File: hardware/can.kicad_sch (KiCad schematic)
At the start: 7 parts, among them U2 MCP2542FDxMF

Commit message: values-correction
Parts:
- C7, C8: value 100nF -> 100n
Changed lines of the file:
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@@
 			)
 		)
-		(property "Value" "100nF"
+		(property "Value" "100n"
 			(at 100.33 84.4613 0)
 			(effects
@@
 			)
 		)
-		(property "Value" "100nF"
+		(property "Value" "100n"
 			(at 133.35 83.8262 0)
 			(effects

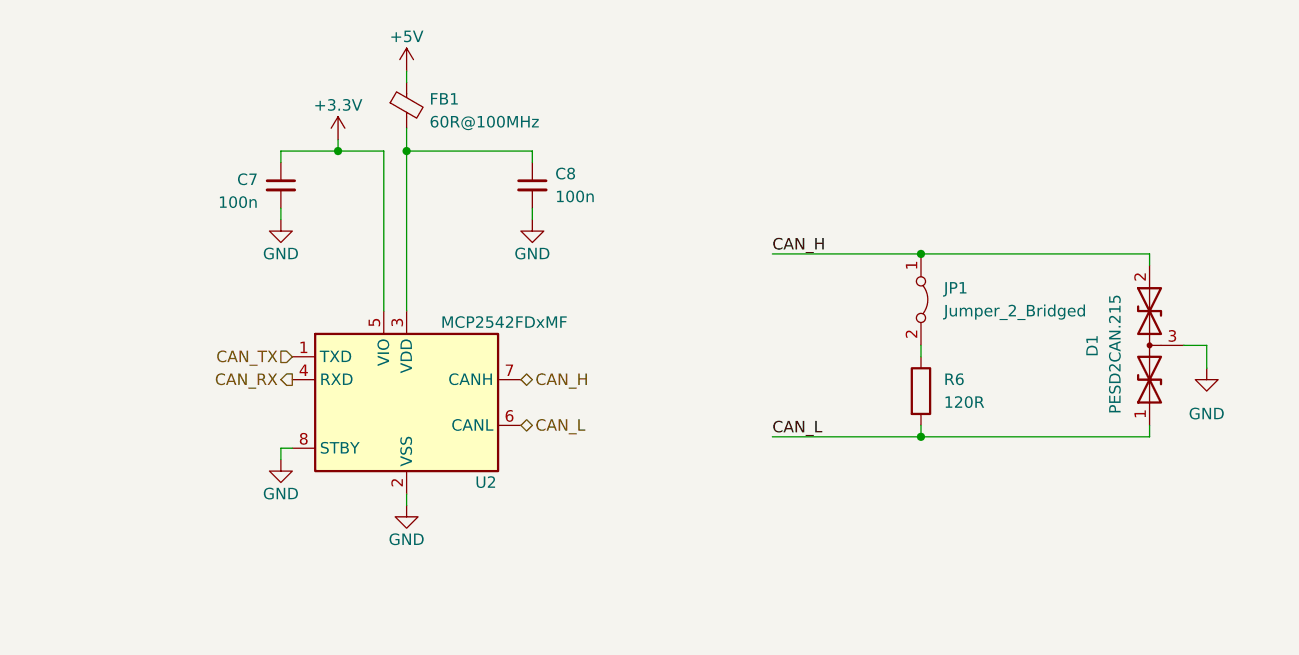
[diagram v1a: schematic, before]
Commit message: added sheet pins
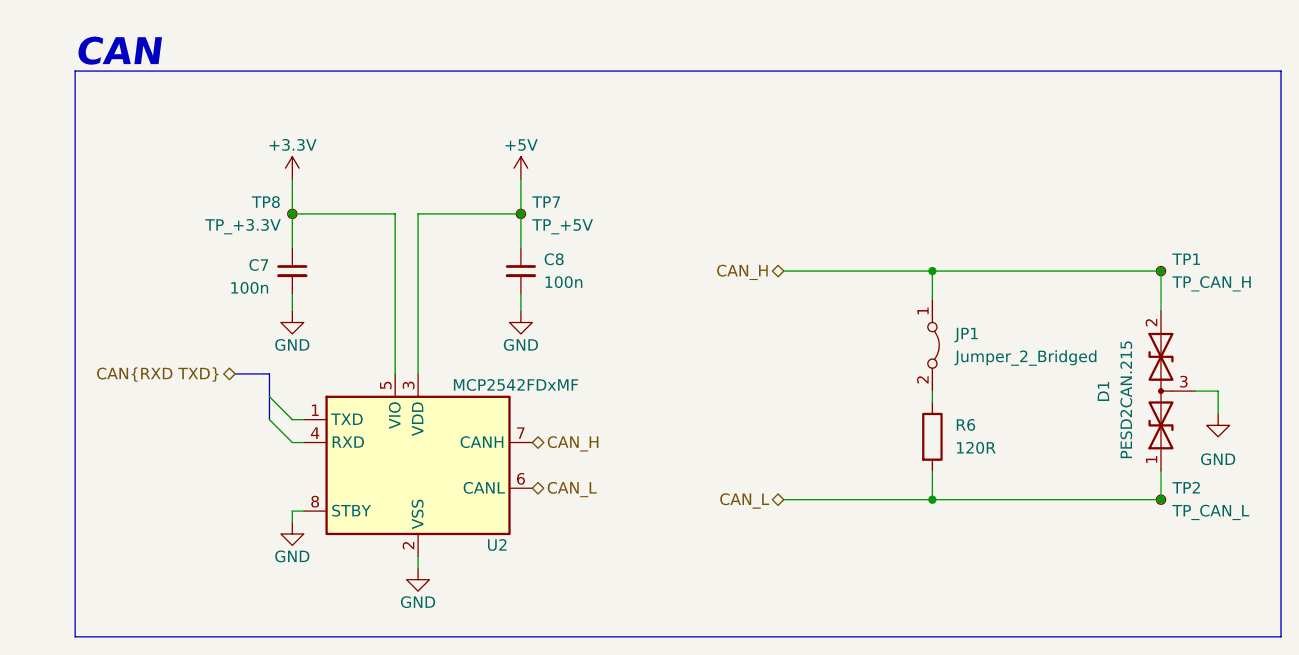
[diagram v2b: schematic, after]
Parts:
- removed FB1: 60R@100MHz, Inductor_SMD:L_0603_1608Metric, symbol Device:FerriteBead_Small
- added TP1: TP_CAN_H, symbol Connector:TestPoint_Small
- added TP2: TP_CAN_L, symbol Connector:TestPoint_Small
- added TP7: TP_+5V, symbol Connector:TestPoint_Small
- added TP8: TP_+3.3V, symbol Connector:TestPoint_Small
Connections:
- net +3.3V: now also TP8.1
- net +5V: now also C8.1, U2.3 (VDD), TP7.1
- net CAN_H: now also TP1.1
- net CAN_L: now also TP2.1
- net CAN_RX: no longer names the net of U2.4 (RXD)
- net CAN_TX: no longer names the net of U2.1 (TXD)
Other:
- note added: "CAN"
- moved on the sheet: C7, C8, D1, JP1, R6, U2

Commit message: added 6V6 for servo
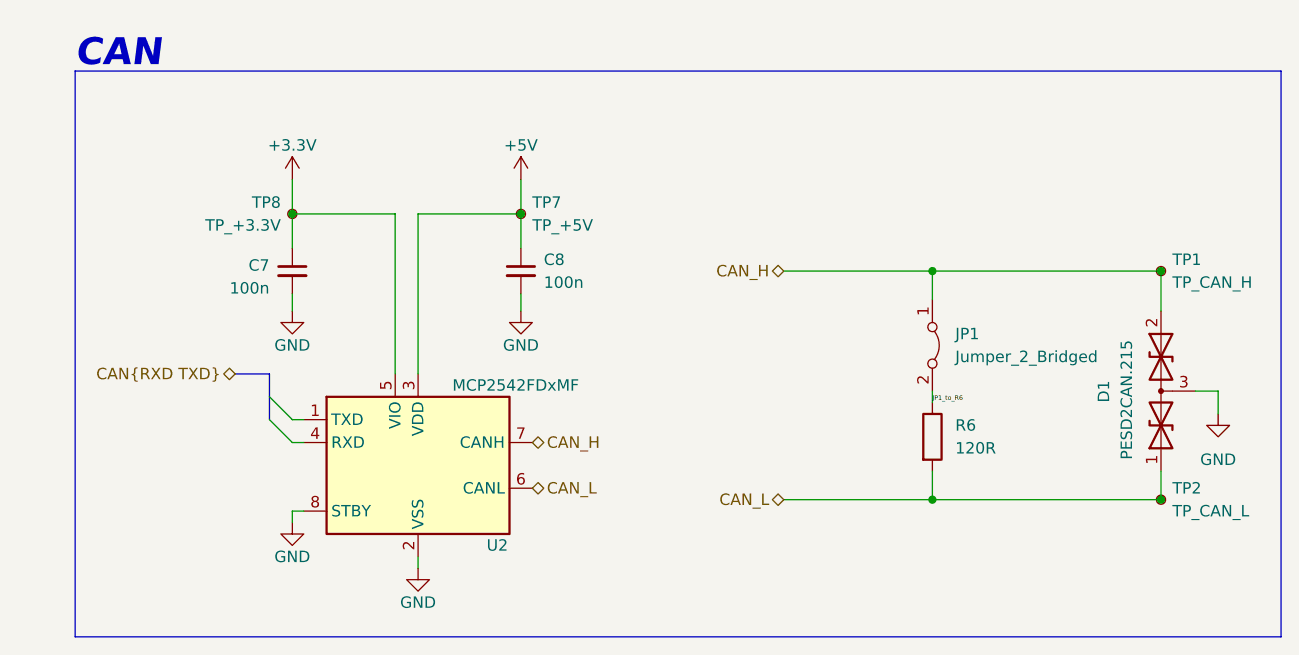
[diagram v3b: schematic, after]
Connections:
- net JP1_to_R6: now reaches JP1.2 (B), R6.1
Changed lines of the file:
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@@
+		)
+	)
+	(label "JP1_to_R6"
+		(at 175.26 106.68 0)
+		(fields_autoplaced yes)
+		(effects
+			(font
+				(size 0.508 0.508)
+			)
+			(justify left bottom)
 		)
 	)

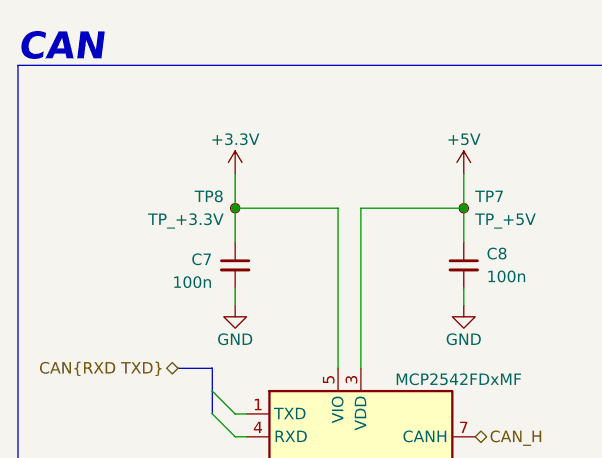
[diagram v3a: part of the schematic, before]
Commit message: connectors - added, buses - todo
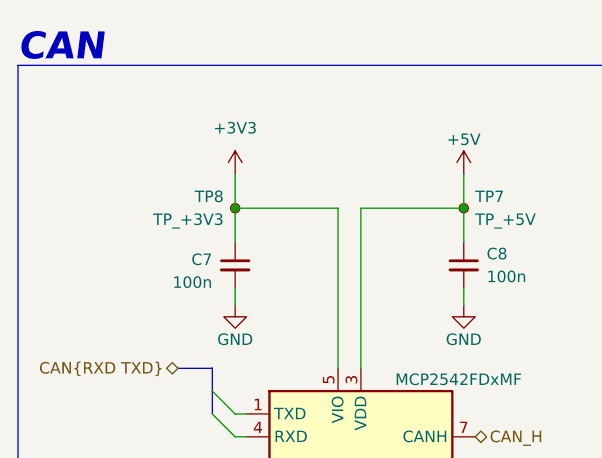
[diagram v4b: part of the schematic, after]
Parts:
- TP8: value TP_+3.3V -> TP_+3V3
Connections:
- net +3.3V renamed +3V3
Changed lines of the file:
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@@
+	)
+	(symbol
+		(lib_id "power:+3V3")
+		(at 104.14 81.915 0)
+		(unit 1)
+		(exclude_from_sim no)
+		(in_bom yes)
+		(on_board yes)
+		(dnp no)
+		(fields_autoplaced yes)
+		(property "Reference" "#PWR014"
+			(at 104.14 85.725 0)
+			(effects
+				(font
+					(size 1.27 1.27)
+				)
+				(hide yes)
+			)
+		)
+		(property "Value" "+3V3"
+			(at 104.14 76.835 0)
+			(effects
+				(font
+					(size 1.27 1.27)
+				)
+			)
+		)
+		(property "Footprint" ""
+			(at 104.14 81.915 0)
+			(effects
+				(font
+					(size 1.27 1.27)
+				)
+				(hide yes)
+			)
+		)
+		(property "Datasheet" ""
+			(at 104.14 81.915 0)
+			(effects
+				(font
+					(size 1.27 1.27)
+				)
+				(hide yes)
+			)
+		)
+		(property "Description" "Power symbol creates a global label with name \"+3V3\""
+			(at 104.14 81.915 0)
+			(effects
+				(font
+					(size 1.27 1.27)
+				)
+				(hide yes)
+			)
+		)
+		(pin "1"
+		)
+		(instances
+			(project "drs"
+				(path "/b652b05a-4e3d-4ad1-b032-18886abe7d45/b1fd2a01-bf35-4031-ba71-28db4e5321a0"
+					(reference "#PWR014")
+					(unit 1)
+				)
+			)
+		)
 	)
 	(symbol
@@
 			)
 		)
-		(property "Value" "TP_+3.3V"
+		(property "Value" "TP_+3V3"
 			(at 102.87 86.9949 0)
 			(effects
@@
 					(unit 1)
 				)
-			)
-		)
-	)
-	(symbol
-		(lib_id "power:+3.3V")
-		(at 104.14 81.915 0)
-		(unit 1)
-		(exclude_from_sim no)
-		(in_bom yes)
-		(on_board yes)
-		(dnp no)
-		(fields_autoplaced yes)
-		(property "Reference" "#PWR014"
-			(at 104.14 85.725 0)
-			(effects
-				(font
-					(size 1.27 1.27)
-				)
-				(hide yes)
-			)
-		)
-		(property "Value" "+3.3V"
-			(at 104.14 78.105 0)
-			(effects
-				(font
-					(size 1.27 1.27)
-				)
-			)
-		)
-		(property "Footprint" ""
-			(at 104.14 81.915 0)
-			(effects
-				(font
-					(size 1.27 1.27)
-				)
-				(hide yes)
-			)
-		)
-		(property "Datasheet" ""
-			(at 104.14 81.915 0)
-			(effects
-				(font
-					(size 1.27 1.27)
-				)
-				(hide yes)
-			)
-		)
-		(property "Description" ""
-			(at 104.14 81.915 0)
-			(effects
-				(font
-					(size 1.27 1.27)
-				)
-				(hide yes)
-			)
-		)
-		(pin "1"
-		)
-		(instances
-			(project "drs"
-				(path "/b652b05a-4e3d-4ad1-b032-18886abe7d45/b1fd2a01-bf35-4031-ba71-28db4e5321a0"
-					(reference "#PWR014")
-					(unit 1)
-				)

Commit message: Poprawione busy, brak errorow
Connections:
- net TXD: now reaches U2.1 (TXD)
- net RXD: now reaches U2.4 (RXD)
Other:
- moved on the sheet: C7, C8, TP1, TP2, TP7, TP8, U2

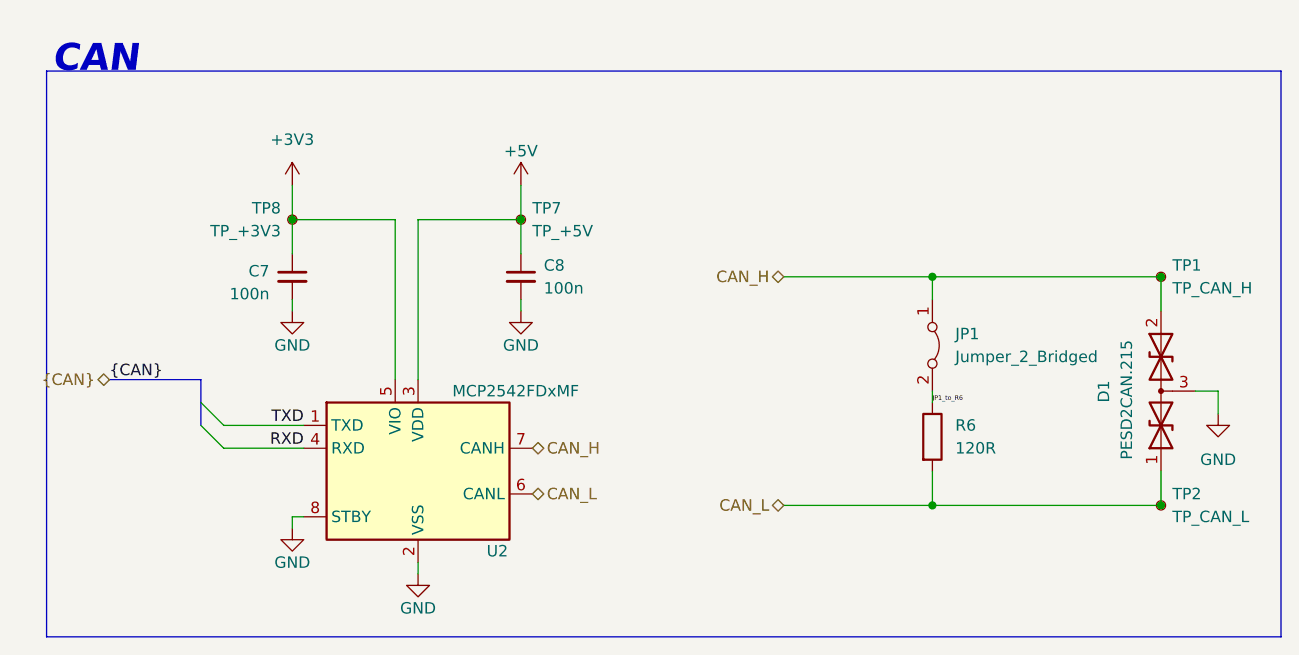
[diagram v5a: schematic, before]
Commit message: Footprints addes beside PWM connectors
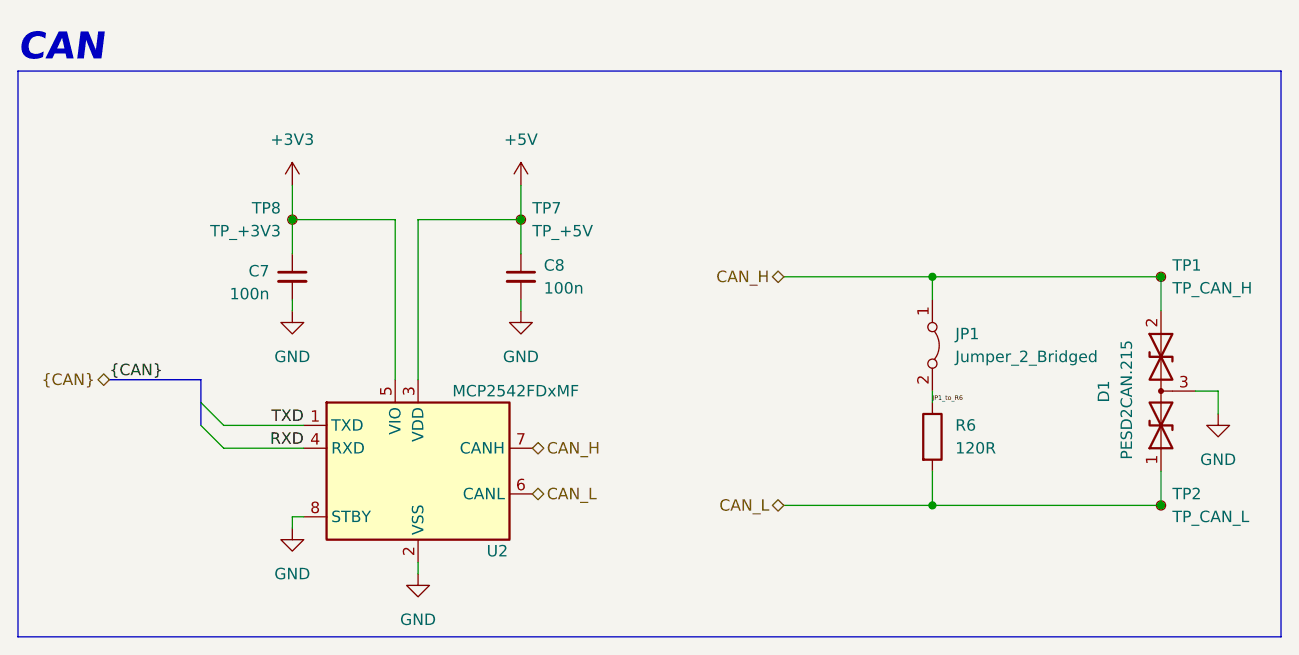
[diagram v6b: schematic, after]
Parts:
- TP1, TP2, TP7, TP8: footprint (none) -> TestPoint:TestPoint_Pad_1.0x1.0mm

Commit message: Table updated- fuses and conns still not added
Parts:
- C7, C8: Mouser Price/Stock (none) -> https://www.mouser.pl/ProductDetail/KEMET/C0603C104J5RACTM?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
- D1: Mouser Price/Stock (none) -> https://www.mouser.pl/ProductDetail/Nexperia/PESD2CAN215?qs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
- R6: Mouser Price/Stock (none) -> https://www.mouser.pl/ProductDetail/ROHM-Semiconductor/SFR0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
- U2: Mouser Price/Stock (none) -> https://www.mouser.pl/ProductDetail/Microchip-Technology/MC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
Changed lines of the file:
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@@
 			)
 		)
-		(property "Datasheet" "~"
+		(property "Datasheet" "https://www.rohm.com/datasheet?p=SFR03EZPJ&dist=Mouser&media=referral&source=mouser.com&campaign=Mouser"
 			(at 175.26 110.49 0)
 			(effects
@@
 		)
 		(property "m" "RK73H1JTTD1200F"
+			(at 175.26 110.49 0)
+			(effects
+				(font
+					(size 1.27 1.27)
+				)
+				(hide yes)
+			)
+		)
+		(property "Mouser Price/Stock" "https://www.mouser.pl/ProductDetail/ROHM-Semiconductor/SFR03EZPJ121?qs=sGAEpiMZZMtlubZbdhIBIONtIqra%2FA5Y7zXrig9MQT8%3D"
 			(at 175.26 110.49 0)
 			(effects
@@
 			)
 		)
-		(property "Datasheet" "~"
+		(property "Datasheet" "https://www.mouser.pl/datasheet/2/447/KEM_C1002_X7R_SMD-3316098.pdf"
 			(at 104.14 92.71 0)
 			(effects
@@
 		)
 		(property "Description" ""
+			(at 104.14 92.71 0)
+			(effects
+				(font
+					(size 1.27 1.27)
+				)
+				(hide yes)
+			)
+		)
+		(property "Mouser Price/Stock" "https://www.mouser.pl/ProductDetail/KEMET/C0603C104J5RACTM?qs=JHaSZE6YWYWxKFeO4jSa6A%3D%3D"
 			(at 104.14 92.71 0)
 			(effects
@@
 			)
 		)
+		(property "Mouser Price/Stock" "https://www.mouser.pl/ProductDetail/Microchip-Technology/MCP2542FDT-H-MF?qs=qdgZG5p0FZ4SFwsOvrAdQg%3D%3D"
+			(at 118.11 114.3 0)
+			(effects
+				(font
+					(size 1.27 1.27)
+				)
+				(hide yes)
+			)
+		)
 		(pin "1"
 		)
@@
 			)
 		)
-		(property "Datasheet" "~"
+		(property "Datasheet" "https://assets.nexperia.com/documents/data-sheet/PESD2CAN.pdf"
 			(at 200.66 109.22 0)
 			(effects
@@
 		)
 		(property "Description" ""
+			(at 200.66 105.41 0)
+			(effects
+				(font
+					(size 1.27 1.27)
+				)
+				(hide yes)
+			)
+		)
+		(property "Mouser Price/Stock" "https://www.mouser.pl/ProductDetail/Nexperia/PESD2CAN215?qs=LOCUfHb8d9sqg7TaLUP2JQ%3D%3D"
 			(at 200.66 105.41 0)
 			(effects
@@
 			)
 		)
-		(property "Datasheet" "~"
+		(property "Datasheet" "https://www.mouser.pl/datasheet/2/447/KEM_C1002_X7R_SMD-3316098.pdf"
 			(at 129.54 92.71 0)
 			(effects
@@
 			(at 129.54 92.71 0)
 			(effects
+				(font
+					(size 1.27 1.27)
+				)
+				(hide yes)
+			)
+		)
+		(property "Mouser Price/Stock" "https://www.mouser.pl/ProductDetail/KEMET/C0603C104J5RACTM?qs=JHaSZE6YWYWxKFeO4jSa6A%3D%3D"
+			(at 129.54 92.71 0)
+			(effects

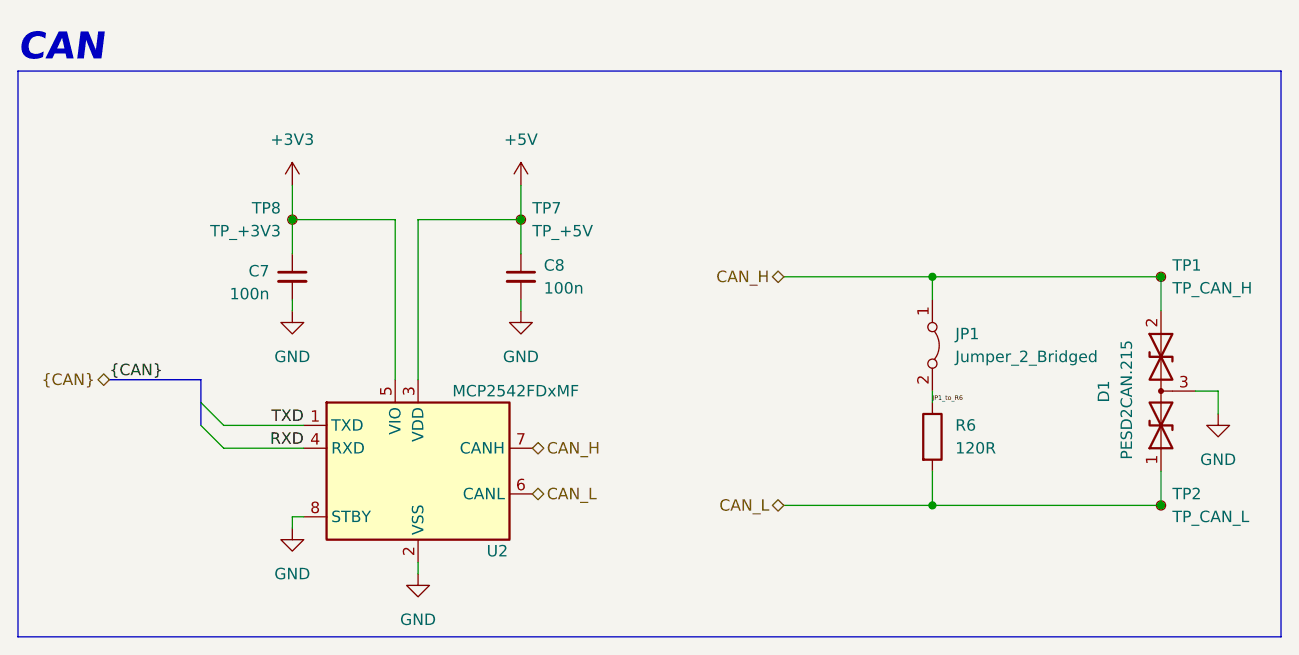
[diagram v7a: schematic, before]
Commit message: pcb scheme update - general/basic aligment
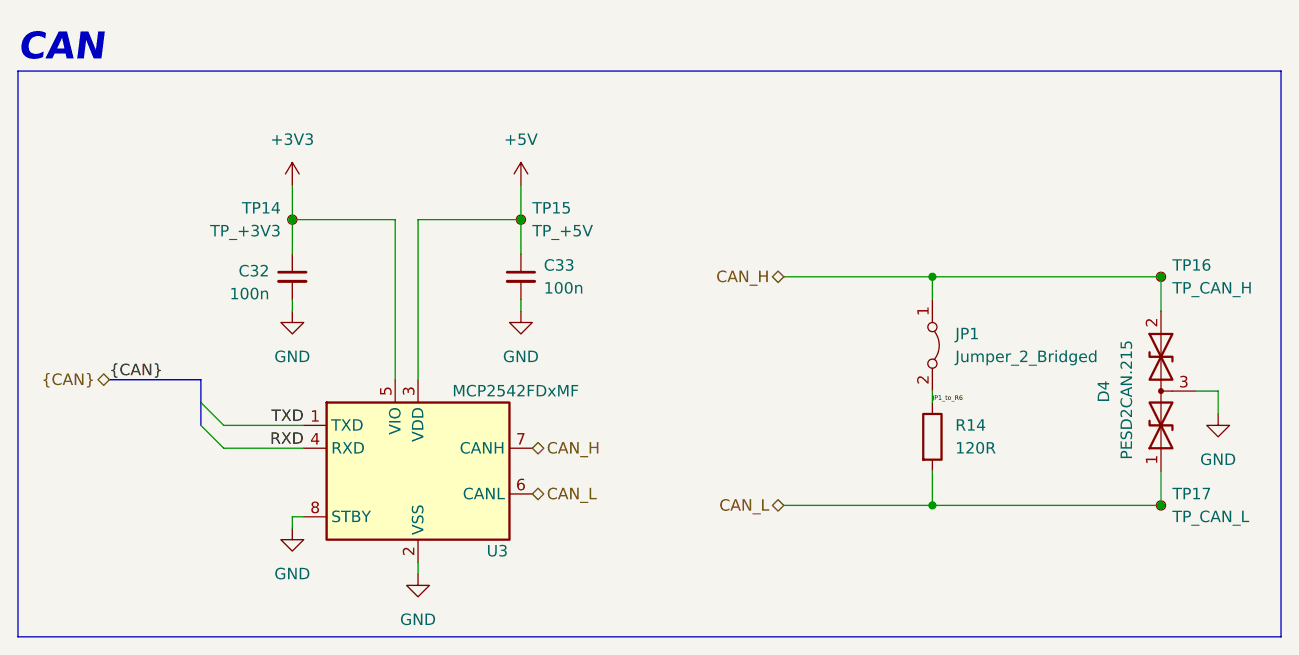
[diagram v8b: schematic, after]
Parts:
- renumbered C7 to C32, C8 to C33, D1 to D4, R6 to R14, TP8 to TP14, TP7 to TP15, TP1 to TP16, TP2 to TP17, U2 to U3
